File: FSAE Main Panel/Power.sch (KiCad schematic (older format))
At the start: 12 parts, among them Q301 IRLML6402TRPBF, U301 ZLDO1117-5V, U302 LP2985-3.3, U303 LM1085-5.0

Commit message: Major Revision
Deleted a ton of routes, Sorry Gary.
Changed all LEDs to 1206s for better brightness
Added a lot of local net names for easier routing
Flipped J203 for better routing
Expanded board outline to fit final dashboard cutout
Added half of the Mounting Holes
Realigned RPM strip
Added Linear Reg Load Resistors to meet minimum current specs
Changed Aux load Linear Regulators to a better one
Added Separate Linear Reg for the DWC
Tuned the CAN Bus differential Pair Lines for equal length
Added decoupling capacitors at a few locations
Rerouted Power traces to be shorter and cleaner
Set up keep out zones for CAN bus interference shielding.
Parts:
- added C307: 1uF, Capacitors_SMD:C_1206, symbol Device:C
- added C308: 100nF, Capacitors_SMD:C_1206, symbol Device:C
- added C309: 47uF, Capacitors_SMD:C_1206, symbol Device:C
- added D302: BYS10-45-E3/TR, Diodes_SMD:D_SMA, symbol Device:D
- added L302: 742792310 Ferrite Bead, Inductors_SMD:L_1210, symbol Device:Ferrite_Bead
- added R301, R302, R303: 909, Resistors_SMD:R_1206, symbol Device:R
- added U304: UA7805CKTTR, Texas_Additions:TO-263-3_TabPin2_PAD_2012, symbol Regulator_Linear:uA7805
- C301: value 4.7uF -> 1uF
- C303: value 4.7uF -> 100nF
- U301: value ZLDO1117-5V -> UA7805CKTTR; footprint TO_SOT_Packages_SMD:TO-252-2 -> Texas_Additions:TO-263-3_TabPin2_PAD_2012; symbol zldo1117-5v:ZLDO1117-5V -> regul:uA7805
- U303: footprint TO_SOT_Packages_SMD:TO-263-3_TabPin2 -> Texas_Additions:TO-263-3_TabPin2_Tab
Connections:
- net +5V: now also U301.3 (OUT), R301.1; no longer U301.2 (VOUT)
- net CAN_V+: now also D302.2 (A)
- net DWC_+5V: now also C308.1, R303.1, U304.3 (OUT); no longer C306.1, U303.2 (VO)
- net GND: now also U301.2 (GND), C307.2, C308.2, C309.2, R301.2, R302.2, R303.2, U304.2 (GND); no longer U301.1 (GND)
- net CAN_D1: now reaches D301.1 (K), L301.2
- net REG1_VIN: now reaches C301.1, L301.1
- net REG1_VIN: now also U301.1 (IN); no longer U301.3 (VIN)
- new net CAN_D2: D302.1 (K), L302.2
- new net LED_+5V: C306.1, C309.1, R302.1, U303.2 (VO)
- new net REG2_VIN: C307.1, L302.1, U304.1 (IN)
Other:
- note added: "DWC Power"
- note removed: "Peak total draw for low power LEDs is 1.2A at 5V\nPeak total draw for high power LEDs is \nPeak total draw for alarm cluster is 800mA at 5V"
- moved on the sheet: C301, C303, C306, D301, L301, U301

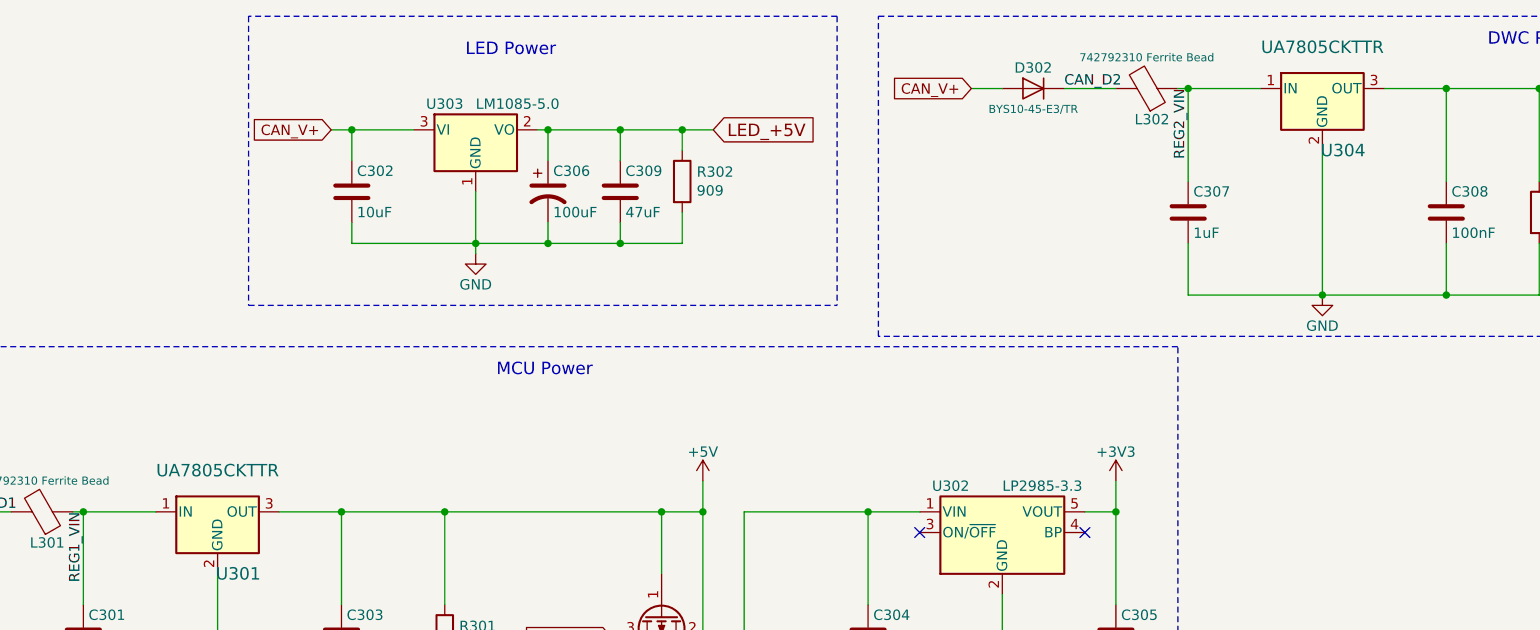
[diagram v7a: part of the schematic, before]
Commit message: Power Supply Changes Again
Shrunk some 5V layout by switching LM7805's for their SOT223 packages but with very careful top copper considerations for thermal management.
Shrunk the Right side by 12mm for more clearance near ignition button.
Fixed Shift Register clock signal routing.
Changed shift order to be 7 segment first for easiler routing.
Added Mounting Holes.
TODO: Figure out Top layer 7 segment placement.
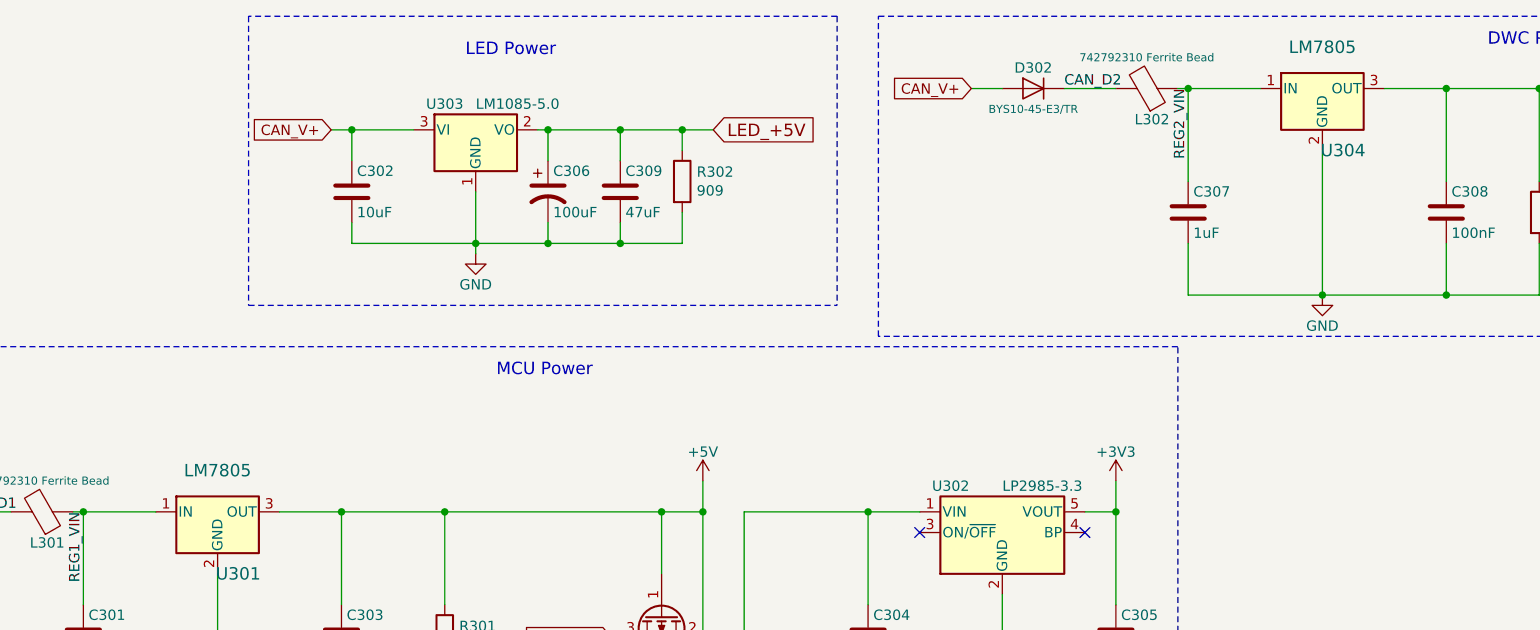
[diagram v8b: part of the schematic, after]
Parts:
- U301, U304: value UA7805CKTTR -> LM7805; footprint Texas_Additions:TO-263-3_TabPin2_PAD_2012 -> TO_SOT_Packages_SMD:SOT-223-3_TabPin2
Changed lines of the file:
@@
 P 3850 4600
 F 0 "U301" H 3950 4300 60  0000 C CNN
-F 1 "UA7805CKTTR" H 3850 4800 60  0000 C CNN
-F 2 "Texas_Additions:TO-263-3_TabPin2_PAD_2012" H 3850 4600 60  0001 C CNN
-F 3 "http://www.ti.com/lit/ds/symlink/ua78.pdf" H 3850 4600 60  0001 C CNN
+F 1 "LM7805" H 3850 4800 60  0000 C CNN
+F 2 "TO_SOT_Packages_SMD:SOT-223-3_TabPin2" H 3850 4600 60  0001 C CNN
+F 3 "http://www.ti.com/lit/ds/symlink/lm340.pdf" H 3850 4600 60  0001 C CNN
 	1    3850 4600
 	1    0    0    -1
@@
 P 9200 2550
 F 0 "U304" H 9300 2250 60  0000 C CNN
-F 1 "UA7805CKTTR" H 9200 2750 60  0000 C CNN
-F 2 "Texas_Additions:TO-263-3_TabPin2_PAD_2012" H 9200 2550 60  0001 C CNN
-F 3 "http://www.ti.com/lit/ds/symlink/ua78.pdf" H 9200 2550 60  0001 C CNN
+F 1 "LM7805" H 9200 2750 60  0000 C CNN
+F 2 "TO_SOT_Packages_SMD:SOT-223-3_TabPin2" H 9200 2550 60  0001 C CNN
+F 3 "http://www.ti.com/lit/ds/symlink/lm340.pdf" H 9200 2550 60  0001 C CNN
 	1    9200 2550
 	1    0    0    -1
